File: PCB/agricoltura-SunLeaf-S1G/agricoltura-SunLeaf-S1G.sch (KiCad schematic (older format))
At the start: 0 parts

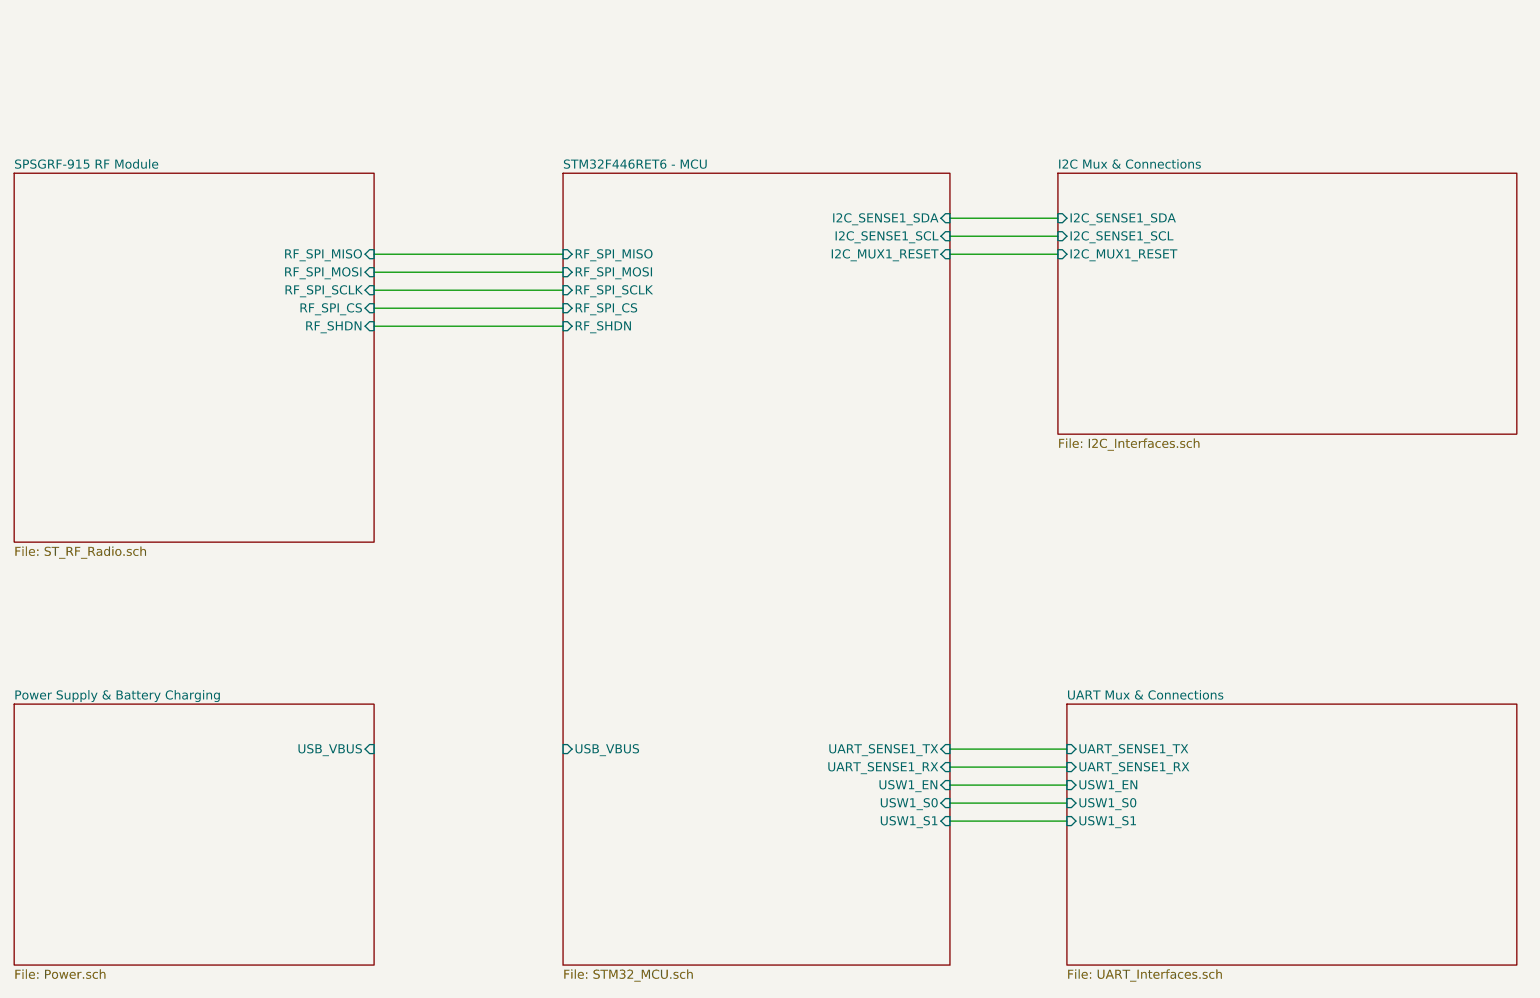
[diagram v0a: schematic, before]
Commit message: Power Supply and Datasheets
Added datasheets for parts in use, designed power supply circuit
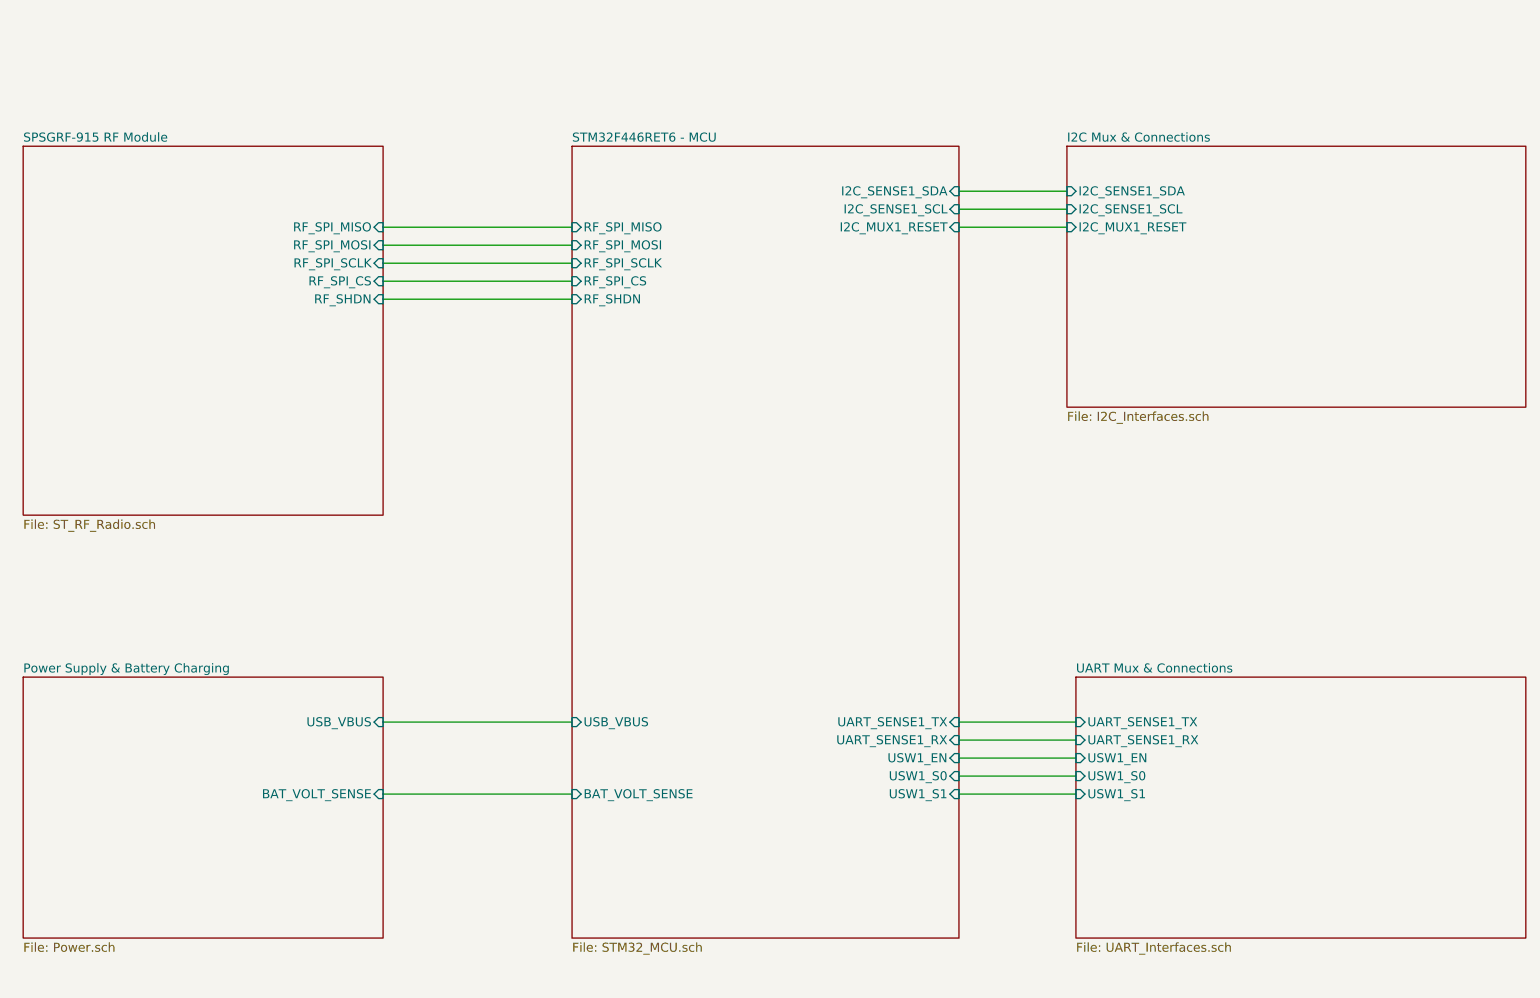
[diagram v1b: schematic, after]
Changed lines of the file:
@@
 $EndDescr
 $Sheet
-S 4750 1800 2150 4400
+S 4800 1650 2150 4400
 U 5F054F9E
 F0 "STM32F446RET6 - MCU" 50
 F1 "STM32_MCU.sch" 50
-F2 "UART_SENSE1_TX" I R 6900 5000 50
-F3 "I2C_SENSE1_SDA" I R 6900 2050 50
-F4 "I2C_SENSE1_SCL" I R 6900 2150 50
-F5 "I2C_MUX1_RESET" I R 6900 2250 50
-F6 "USW1_EN" I R 6900 5200 50
-F7 "USW1_S0" I R 6900 5300 50
-F8 "USW1_S1" I R 6900 5400 50
-F9 "UART_SENSE1_RX" I R 6900 5100 50
-F10 "RF_SHDN" I L 4750 2650 50
-F11 "RF_SPI_CS" I L 4750 2550 50
-F12 "RF_SPI_MOSI" I L 4750 2350 50
-F13 "RF_SPI_MISO" I L 4750 2250 50
-F14 "RF_SPI_SCLK" I L 4750 2450 50
-F15 "USB_VBUS" I L 4750 5000 50
+F2 "UART_SENSE1_TX" I R 6950 4850 50
+F3 "I2C_SENSE1_SDA" I R 6950 1900 50
+F4 "I2C_SENSE1_SCL" I R 6950 2000 50
+F5 "I2C_MUX1_RESET" I R 6950 2100 50
+F6 "USW1_EN" I R 6950 5050 50
+F7 "USW1_S0" I R 6950 5150 50
+F8 "USW1_S1" I R 6950 5250 50
+F9 "UART_SENSE1_RX" I R 6950 4950 50
+F10 "RF_SHDN" I L 4800 2500 50
+F11 "RF_SPI_CS" I L 4800 2400 50
+F12 "RF_SPI_MOSI" I L 4800 2200 50
+F13 "RF_SPI_MISO" I L 4800 2100 50
+F14 "RF_SPI_SCLK" I L 4800 2300 50
+F15 "USB_VBUS" I L 4800 4850 50
+F16 "BAT_VOLT_SENSE" I L 4800 5250 50
 $EndSheet
 $Sheet
-S 1700 1800 2000 2050
+S 1750 1650 2000 2050
 U 5F055094
 F0 "SPSGRF-915 RF Module " 50
 F1 "ST_RF_Radio.sch" 50
-F2 "RF_SHDN" I R 3700 2650 50
-F3 "RF_SPI_CS" I R 3700 2550 50
-F4 "RF_SPI_MOSI" I R 3700 2350 50
-F5 "RF_SPI_MISO" I R 3700 2250 50
-F6 "RF_SPI_SCLK" I R 3700 2450 50
+F2 "RF_SHDN" I R 3750 2500 50
+F3 "RF_SPI_CS" I R 3750 2400 50
+F4 "RF_SPI_MOSI" I R 3750 2200 50
+F5 "RF_SPI_MISO" I R 3750 2100 50
+F6 "RF_SPI_SCLK" I R 3750 2300 50
 $EndSheet
 $Sheet
-S 1700 4750 2000 1450
+S 1750 4600 2000 1450
 U 5F055222
 F0 "Power Supply & Battery Charging" 50
 F1 "Power.sch" 50
-F2 "USB_VBUS" I R 3700 5000 50
+F2 "USB_VBUS" I R 3750 4850 50
+F3 "BAT_VOLT_SENSE" I R 3750 5250 50
 $EndSheet
 $Sheet
-S 7500 1800 2550 1450
+S 7550 1650 2550 1450
 U 5F0552DA
 F0 "I2C Mux & Connections" 50
 F1 "I2C_Interfaces.sch" 50
-F2 "I2C_SENSE1_SDA" I L 7500 2050 50
-F3 "I2C_SENSE1_SCL" I L 7500 2150 50
-F4 "I2C_MUX1_RESET" I L 7500 2250 50
+F2 "I2C_SENSE1_SDA" I L 7550 1900 50
+F3 "I2C_SENSE1_SCL" I L 7550 2000 50
+F4 "I2C_MUX1_RESET" I L 7550 2100 50
 $EndSheet
 $Sheet
-S 7550 4750 2500 1450
+S 7600 4600 2500 1450
 U 5F05538C
 F0 "UART Mux & Connections" 50
 F1 "UART_Interfaces.sch" 50
-F2 "UART_SENSE1_TX" I L 7550 5000 50
-F3 "UART_SENSE1_RX" I L 7550 5100 50
-F4 "USW1_S1" I L 7550 5400 50
-F5 "USW1_S0" I L 7550 5300 50
-F6 "USW1_EN" I L 7550 5200 50
+F2 "UART_SENSE1_TX" I L 7600 4850 50
+F3 "UART_SENSE1_RX" I L 7600 4950 50
+F4 "USW1_S1" I L 7600 5250 50
+F5 "USW1_S0" I L 7600 5150 50
+F6 "USW1_EN" I L 7600 5050 50
 $EndSheet
 Wire Wire Line
-	4750 2650 3700 2650
+	4800 2500 3750 2500
 Wire Wire Line
-	3700 2550 4750 2550
+	3750 2400 4800 2400
 Wire Wire Line
-	3700 2450 4750 2450
+	3750 2300 4800 2300
 Wire Wire Line
-	4750 2350 3700 2350
+	4800 2200 3750 2200
 Wire Wire Line
-	3700 2250 4750 2250
+	3750 2100 4800 2100
 Wire Wire Line
-	6900 2050 7500 2050
+	6950 1900 7550 1900
 Wire Wire Line
-	7500 2150 6900 2150
+	7550 2000 6950 2000
 Wire Wire Line
-	6900 2250 7500 2250
+	6950 2100 7550 2100
 Wire Wire Line
-	6900 5000 7550 5000
+	6950 4850 7600 4850
 Wire Wire Line
-	7550 5100 6900 5100
+	7600 4950 6950 4950
 Wire Wire Line
-	6900 5300 7550 5300
+	6950 5150 7600 5150
 Wire Wire Line
-	6900 5200 7550 5200
+	6950 5050 7600 5050
 Wire Wire Line
-	7550 5400 6900 5400
+	7600 5250 6950 5250
+Wire Wire Line
+	3750 4850 4800 4850
+Wire Wire Line
+	4800 5250 3750 5250
 $EndSCHEMATC

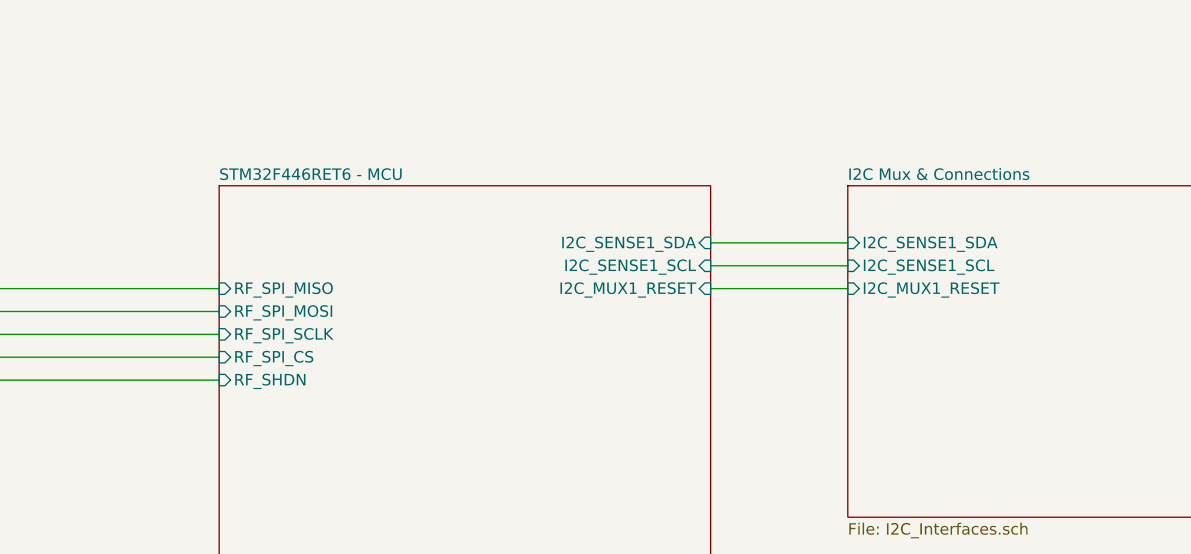
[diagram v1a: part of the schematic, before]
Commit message: Schematic Complete
Schematic completed and PCB started
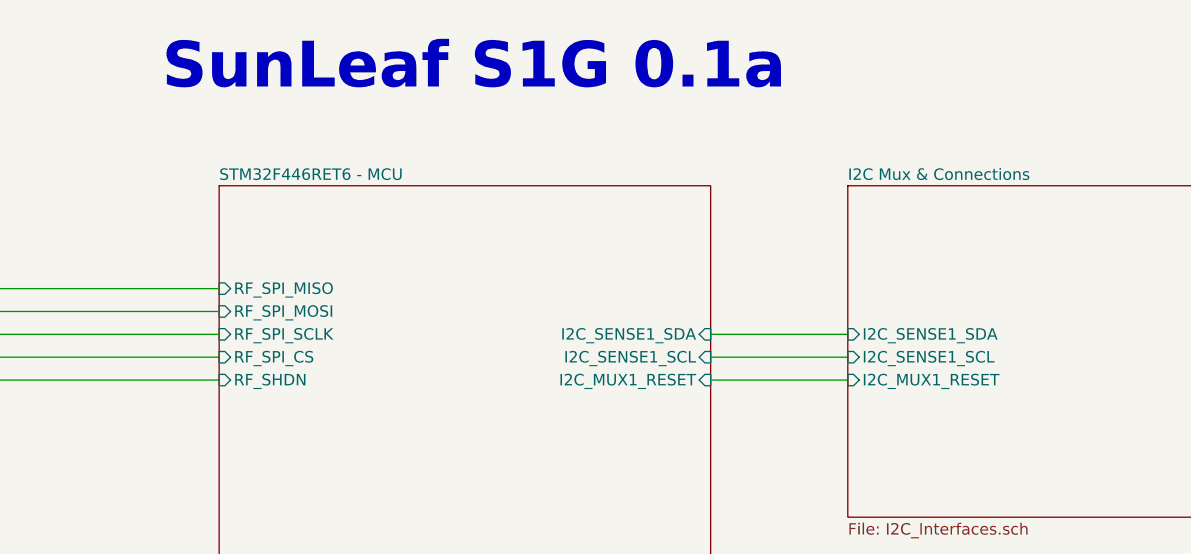
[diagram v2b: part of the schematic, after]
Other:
- note added: "SunLeaf S1G 0.1a"
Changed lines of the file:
@@
 F1 "STM32_MCU.sch" 50
 F2 "UART_SENSE1_TX" I R 6950 4850 50
-F3 "I2C_SENSE1_SDA" I R 6950 1900 50
-F4 "I2C_SENSE1_SCL" I R 6950 2000 50
-F5 "I2C_MUX1_RESET" I R 6950 2100 50
+F3 "I2C_SENSE1_SDA" I R 6950 2300 50
+F4 "I2C_SENSE1_SCL" I R 6950 2400 50
+F5 "I2C_MUX1_RESET" I R 6950 2500 50
 F6 "USW1_EN" I R 6950 5050 50
 F7 "USW1_S0" I R 6950 5150 50
@@
 F0 "I2C Mux & Connections" 50
 F1 "I2C_Interfaces.sch" 50
-F2 "I2C_SENSE1_SDA" I L 7550 1900 50
-F3 "I2C_SENSE1_SCL" I L 7550 2000 50
-F4 "I2C_MUX1_RESET" I L 7550 2100 50
+F2 "I2C_SENSE1_SDA" I L 7550 2300 50
+F3 "I2C_SENSE1_SCL" I L 7550 2400 50
+F4 "I2C_MUX1_RESET" I L 7550 2500 50
 $EndSheet
 $Sheet
@@
 	3750 2100 4800 2100
 Wire Wire Line
-	6950 1900 7550 1900
+	6950 2300 7550 2300
 Wire Wire Line
-	7550 2000 6950 2000
+	7550 2400 6950 2400
 Wire Wire Line
-	6950 2100 7550 2100
+	6950 2500 7550 2500
 Wire Wire Line
 	6950 4850 7600 4850
@@
 Wire Wire Line
 	4800 5250 3750 5250
+Text Notes 4550 1250 0    200  ~ 40
+SunLeaf S1G 0.1a
 $EndSCHEMATC

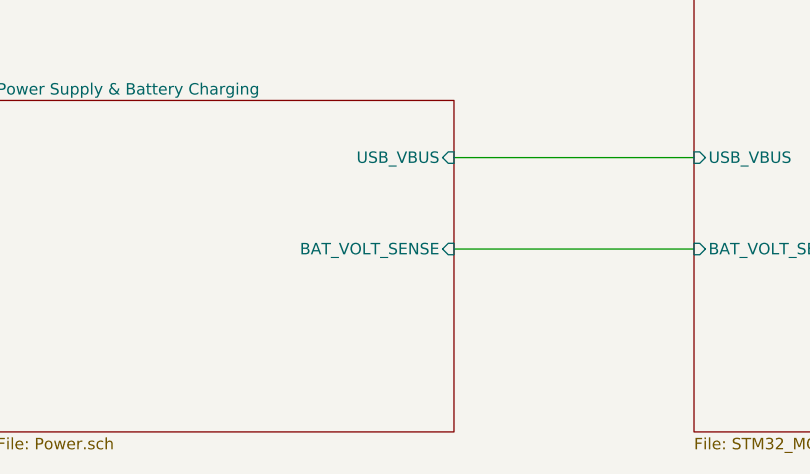
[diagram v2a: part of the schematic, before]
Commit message: Pullups
Added pullup reistors to I2C ports, changed JTAG connector over to Tag connect.
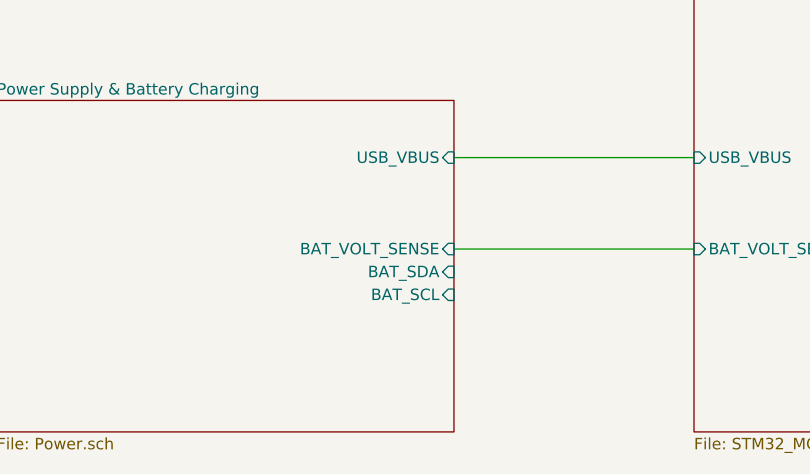
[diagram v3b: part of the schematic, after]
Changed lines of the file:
@@
 F2 "USB_VBUS" I R 3750 4850 50
 F3 "BAT_VOLT_SENSE" I R 3750 5250 50
+F4 "BAT_SDA" I R 3750 5350 50
+F5 "BAT_SCL" I R 3750 5450 50
 $EndSheet
 $Sheet

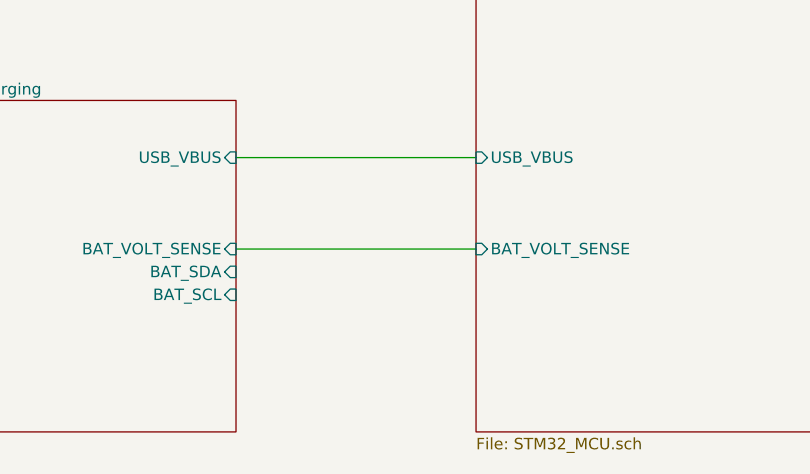
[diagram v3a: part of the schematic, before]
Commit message: PCB Progress
PCB routing progress made, USB port replaced with micro b like older sunleaf designs.
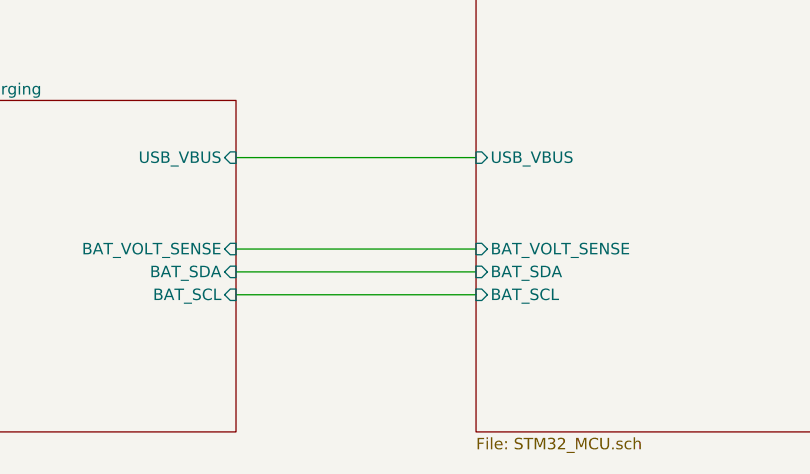
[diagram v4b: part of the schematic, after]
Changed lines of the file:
@@
 F15 "USB_VBUS" I L 4800 4850 50
 F16 "BAT_VOLT_SENSE" I L 4800 5250 50
+F17 "BAT_SDA" I L 4800 5350 50
+F18 "BAT_SCL" I L 4800 5450 50
 $EndSheet
 $Sheet
@@
 Text Notes 4550 1250 0    200  ~ 40
 SunLeaf S1G 0.1a
+Wire Wire Line
+	3750 5350 4800 5350
+Wire Wire Line
+	4800 5450 3750 5450
 $EndSCHEMATC
